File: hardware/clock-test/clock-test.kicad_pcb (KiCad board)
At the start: 2 copper layers, 99.8 x 99.8 mm, 78 parts, among them J3 S7 Mini, J4 S7 Mini

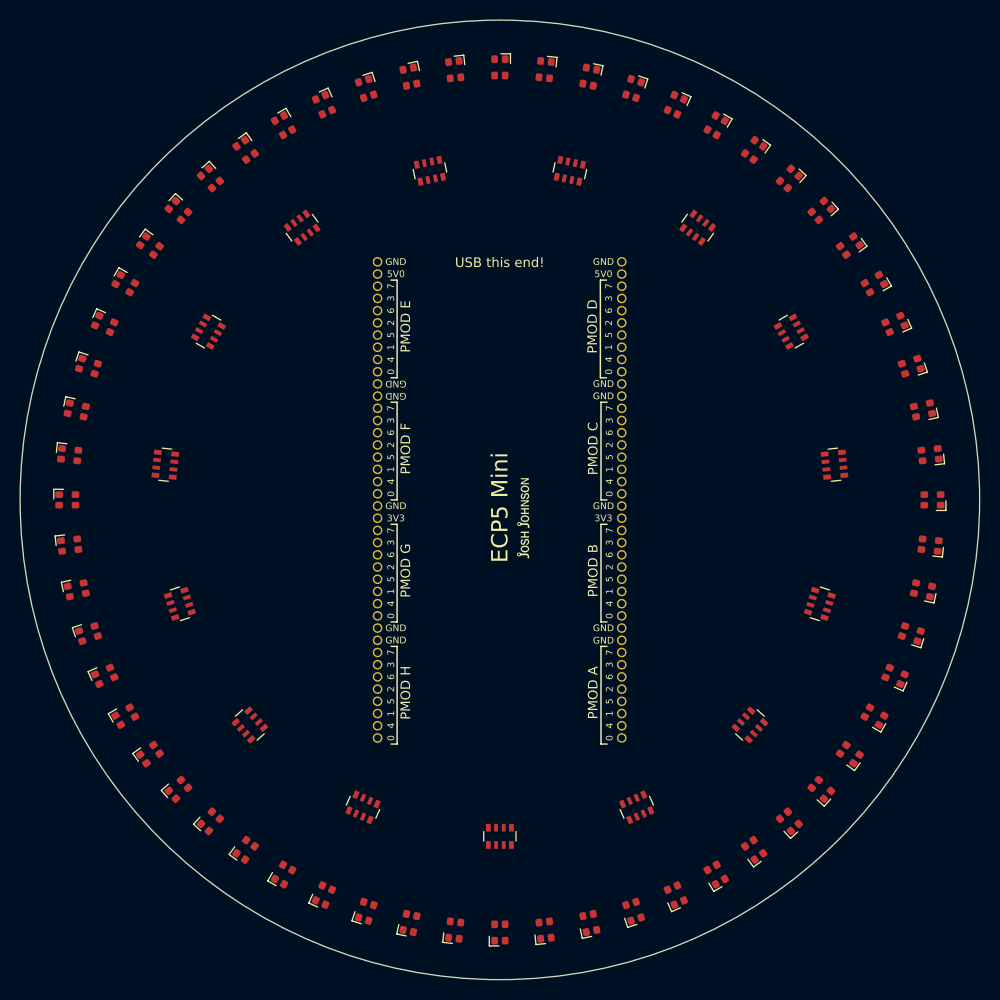
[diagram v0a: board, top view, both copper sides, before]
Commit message: clock-test laid out
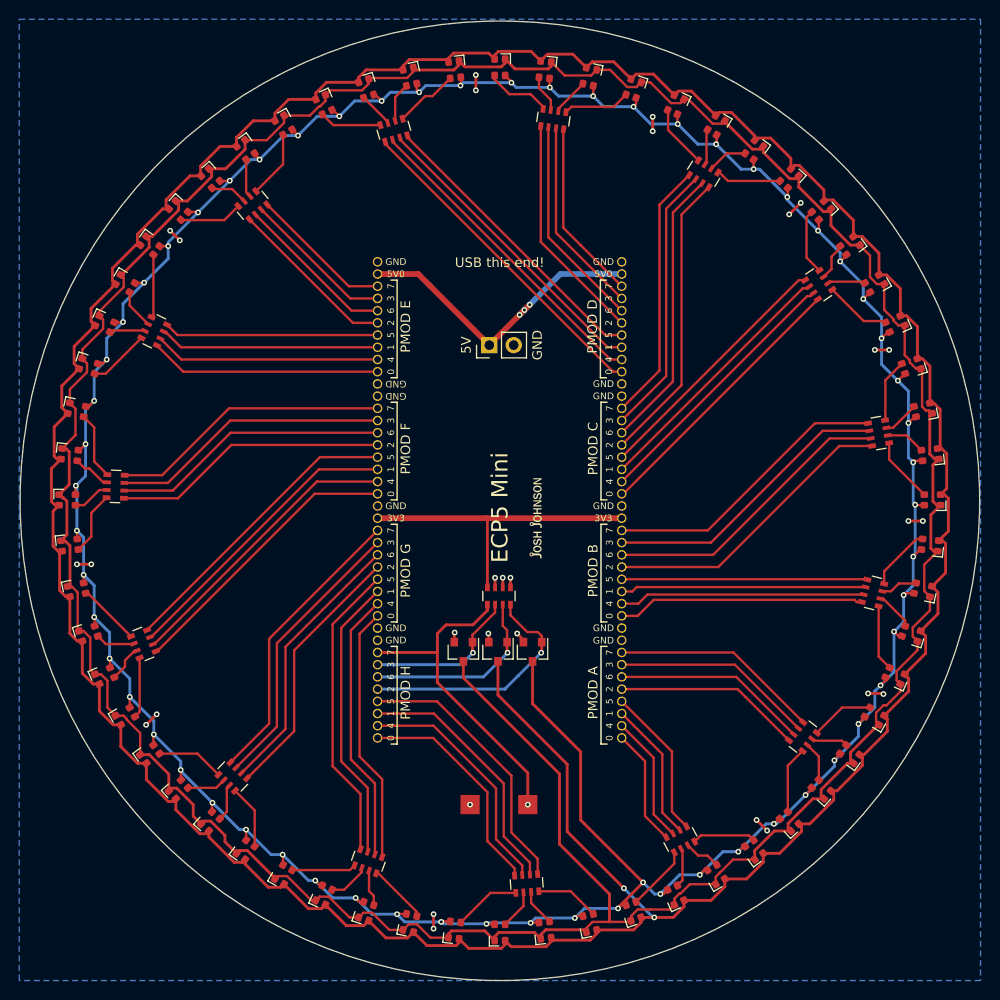
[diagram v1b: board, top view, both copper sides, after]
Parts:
- added J1: PWR, Connector_PinHeader_2.54mm:PinHeader_1x02_P2.54mm_Vertical, F.Cu at (148.9, 83.9)
- added Q1: DMG2302U, Package_TO_SOT_SMD:SOT-23, F.Cu at (146.2, 115.8)
- added Q2: DMG2302U, Package_TO_SOT_SMD:SOT-23, F.Cu at (149.8, 115.8)
- added Q3: DMG2302U, Package_TO_SOT_SMD:SOT-23, F.Cu at (153.4, 115.8)
- added RN16: 10K, Resistor_SMD:R_Array_Convex_4x0603, F.Cu at (149.9, 110.0)
- added SW1: SW_Push, josh-buttons-switches:Switch_SMT_SKPMAPE010, F.Cu at (152.9, 131.7)
- moved RN2 5.64 mm to (181.5, 124.6), turned to 142 degrees
- moved RN8 5.64 mm to (110.0, 98.6), turned to -2 degrees
- moved RN10 5.64 mm to (124.3, 69.4), turned to -50 degrees
- moved RN15 5.64 mm to (189.4, 93.1), turned to -170 degrees
- moved RN6 5.64 mm to (122.2, 128.8), turned to 46 degrees
- moved RN1 5.64 mm to (188.8, 109.7), turned to 166 degrees
- moved RN13 5.64 mm to (171.2, 66.1), turned to -122 degrees
- moved RN7 5.64 mm to (112.9, 115.0), turned to 22 degrees
- moved RN3 5.64 mm to (168.8, 135.3), turned to 118 degrees
- moved RN4 5.64 mm to (152.8, 139.9), turned to 94 degrees
- moved RN14 5.64 mm to (183.2, 77.6), turned to -146 degrees
- moved RN11 5.64 mm to (139.0, 61.5), turned to -74 degrees
- moved RN9 5.64 mm to (114.0, 82.5), turned to -26 degrees
- moved RN12 5.64 mm to (155.6, 60.4), turned to -98 degrees
- moved RN5 5.64 mm to (136.3, 137.6), turned to 70 degrees
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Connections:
- RN1 pad 5: Net-(RN1-Pad5) -> /PORT_B5
- RN1 pad 6: Net-(RN1-Pad6) -> /PORT_B1
- RN1 pad 7: Net-(RN1-Pad7) -> /PORT_B4
- RN1 pad 8: Net-(RN1-Pad8) -> /PORT_B0
- RN10 pad 5: Net-(RN10-Pad5) -> /PORT_E2
- RN10 pad 6: Net-(RN10-Pad6) -> /PORT_E6
- RN10 pad 7: Net-(RN10-Pad7) -> /PORT_E3
- RN10 pad 8: Net-(RN10-Pad8) -> /PORT_E7
- RN11 pad 5: Net-(RN11-Pad5) -> /PORT_D0
- RN11 pad 6: Net-(RN11-Pad6) -> /PORT_D4
- RN11 pad 7: Net-(RN11-Pad7) -> /PORT_D1
- RN11 pad 8: Net-(RN11-Pad8) -> /PORT_D5
- RN12 pad 5: Net-(RN12-Pad5) -> /PORT_D2
- RN12 pad 6: Net-(RN12-Pad6) -> /PORT_D6
- RN12 pad 7: Net-(RN12-Pad7) -> /PORT_D3
- RN12 pad 8: Net-(RN12-Pad8) -> /PORT_D7
- RN13 pad 5: Net-(RN13-Pad5) -> /PORT_C7
- RN13 pad 6: Net-(RN13-Pad6) -> /PORT_C3
- RN13 pad 7: Net-(RN13-Pad7) -> /PORT_C6
- RN13 pad 8: Net-(RN13-Pad8) -> /PORT_C2
- RN14 pad 5: Net-(RN14-Pad5) -> /PORT_C5
- RN14 pad 6: Net-(RN14-Pad6) -> /PORT_C1
- RN14 pad 7: Net-(RN14-Pad7) -> /PORT_C4
- RN14 pad 8: Net-(RN14-Pad8) -> /PORT_C0
- RN15 pad 5: Net-(RN15-Pad5) -> /PORT_B7
- RN15 pad 6: Net-(RN15-Pad6) -> /PORT_B3
- RN15 pad 7: Net-(RN15-Pad7) -> /PORT_B6
- RN15 pad 8: Net-(RN15-Pad8) -> /PORT_B2
- RN2 pad 5: Net-(RN2-Pad5) -> /PORT_A7
- RN2 pad 6: Net-(RN2-Pad6) -> /PORT_A3
- RN2 pad 7: Net-(RN2-Pad7) -> /PORT_A6
- RN2 pad 8: Net-(RN2-Pad8) -> /PORT_A2
- RN3 pad 5: Net-(RN3-Pad5) -> /PORT_A5
- RN3 pad 6: Net-(RN3-Pad6) -> /PORT_A1
- RN3 pad 7: Net-(RN3-Pad7) -> /PORT_A4
- RN3 pad 8: Net-(RN3-Pad8) -> /PORT_A0
- RN4 pad 5: Net-(RN4-Pad5) -> /PORT_H5
- RN4 pad 6: Net-(RN4-Pad6) -> /PORT_H1
- RN4 pad 7: Net-(RN4-Pad7) -> /PORT_H4
- RN4 pad 8: Net-(RN4-Pad8) -> /PORT_H0
- RN5 pad 5: Net-(RN5-Pad5) -> /PORT_G0
- RN5 pad 6: Net-(RN5-Pad6) -> /PORT_G4
- RN5 pad 7: Net-(RN5-Pad7) -> /PORT_G1
- RN5 pad 8: Net-(RN5-Pad8) -> /PORT_G5
- RN6 pad 5: Net-(RN6-Pad5) -> /PORT_G2
- RN6 pad 6: Net-(RN6-Pad6) -> /PORT_G6
- RN6 pad 7: Net-(RN6-Pad7) -> /PORT_G3
- RN6 pad 8: Net-(RN6-Pad8) -> /PORT_G7
- RN7 pad 5: Net-(RN7-Pad5) -> /PORT_F0
- RN7 pad 6: Net-(RN7-Pad6) -> /PORT_F4
- RN7 pad 7: Net-(RN7-Pad7) -> /PORT_F1
- RN7 pad 8: Net-(RN7-Pad8) -> /PORT_F5
- RN8 pad 5: Net-(RN8-Pad5) -> /PORT_F2
- RN8 pad 6: Net-(RN8-Pad6) -> /PORT_F6
- RN8 pad 7: Net-(RN8-Pad7) -> /PORT_F3
- RN8 pad 8: Net-(RN8-Pad8) -> /PORT_F7
- RN9 pad 5: Net-(RN9-Pad5) -> /PORT_E0
- RN9 pad 6: Net-(RN9-Pad6) -> /PORT_E4
- RN9 pad 7: Net-(RN9-Pad7) -> /PORT_E1
- RN9 pad 8: Net-(RN9-Pad8) -> /PORT_E5
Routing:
- net /CAT_B: track 0.00 -> 378.0 mm, vias 0 -> 61
- net /CAT_G: track 0.00 -> 372.2 mm, vias 0 -> 2
- net /CAT_R: track 0.00 -> 365.8 mm
- net /PORT_H7: track 0.00 -> 34.7 mm, vias 0 -> 1
- net /PORT_D0: track 0.00 -> 34.6 mm
- net /PORT_D4: track 0.00 -> 33.4 mm
- net +5V: track 0.00 -> 33.0 mm, vias 0 -> 3
- net +3V3: track 0.00 -> 32.7 mm
- net /PORT_D1: track 0.00 -> 32.2 mm
- net /PORT_F5: track 0.00 -> 31.4 mm
- net /PORT_B2: track 0.00 -> 31.3 mm
- net /PORT_G5: track 0.00 -> 31.2 mm
- net /PORT_D5: track 0.00 -> 31.0 mm
- net /PORT_B6: track 0.00 -> 30.9 mm
- net /PORT_F1: track 0.00 -> 30.9 mm
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- added copper zone on B.Cu, net GND
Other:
- board text added: "5V"

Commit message: clean up routing
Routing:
- net /CAT_G: track 372.2 -> 369.3 mm
- net /CAT_R: track 365.8 -> 363.3 mm
- net GND: track 23.1 -> 23.8 mm

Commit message: update readme following r0.1 bringup
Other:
- board text added: "JLCJLCJLC"
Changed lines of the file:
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@@
   (gr_line (start 139.3085 115.24) (end 138.6735 115.24) (layer "F.SilkS") (width 0.15))
   (gr_circle (center 150 100.093588) (end 199.9 99.293588) (layer "Edge.Cuts") (width 0.1))
+  (gr_text "JLCJLCJLC" (at 149.982499 148.7475) (layer "B.SilkS")
+    (effects (font (size 1 1) (thickness 0.15)) (justify mirror))
+  )
   (gr_text "5" (at 138.6735 95.555 90) (layer "F.SilkS")
     (effects (font (size 0.7 0.7) (thickness 0.12)))
